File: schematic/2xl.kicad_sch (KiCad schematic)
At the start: 79 parts, among them J1 eye, J10 head+, J3 B-, J4 M-, J5 M+, J6 B+, J7 W, J9 head-, Q1 9014C, Q10 9014C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

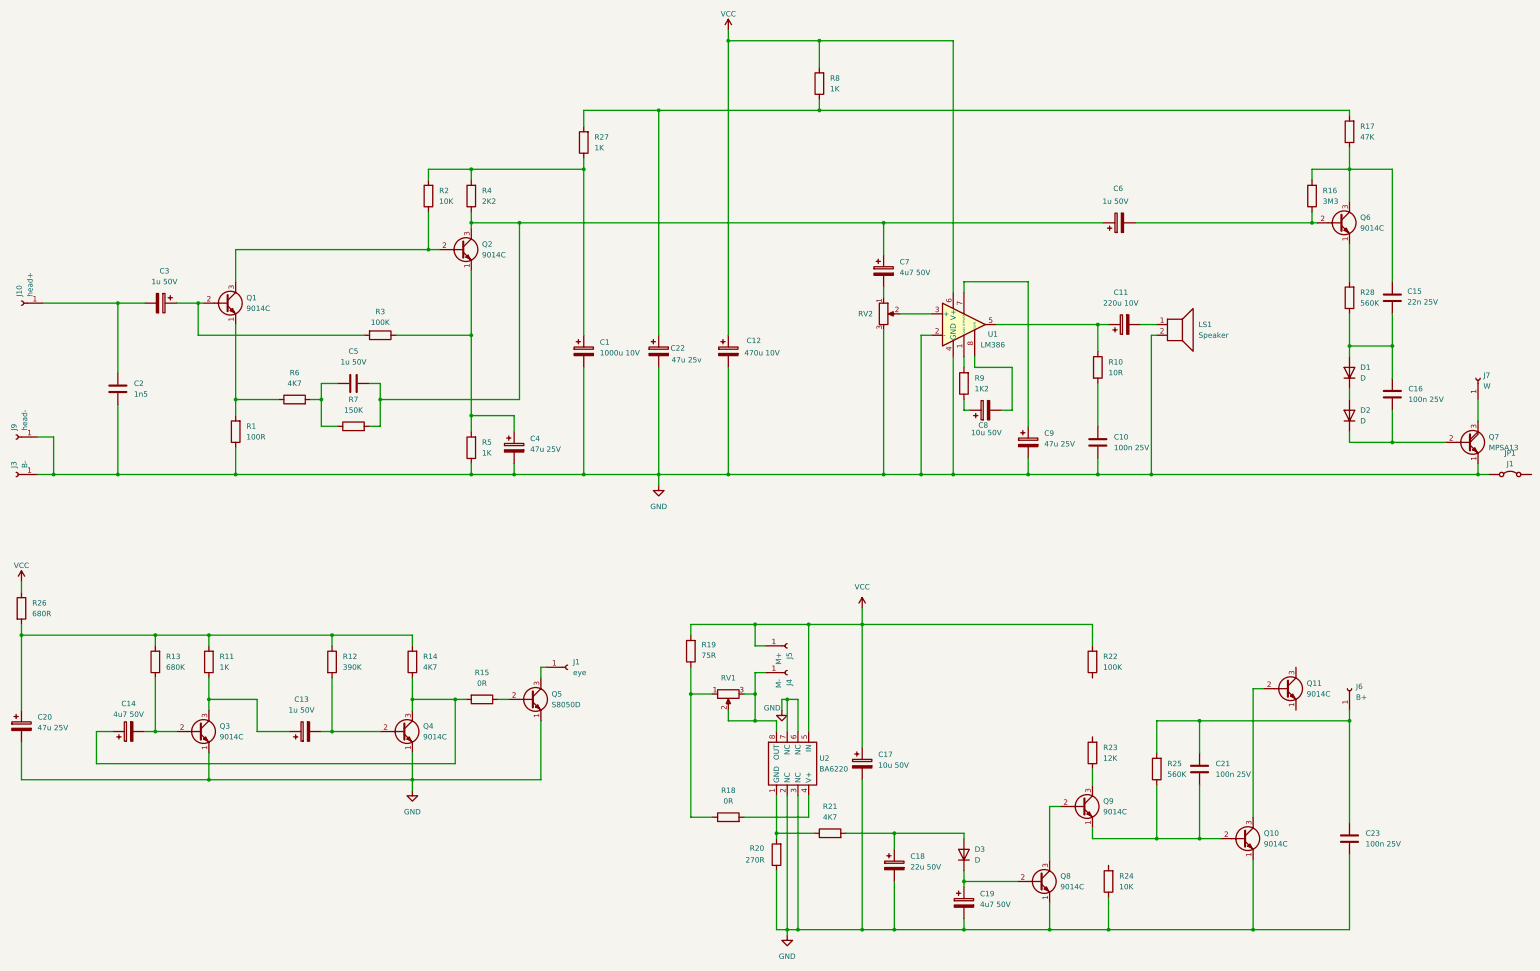
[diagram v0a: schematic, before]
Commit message: rearranged oscillator
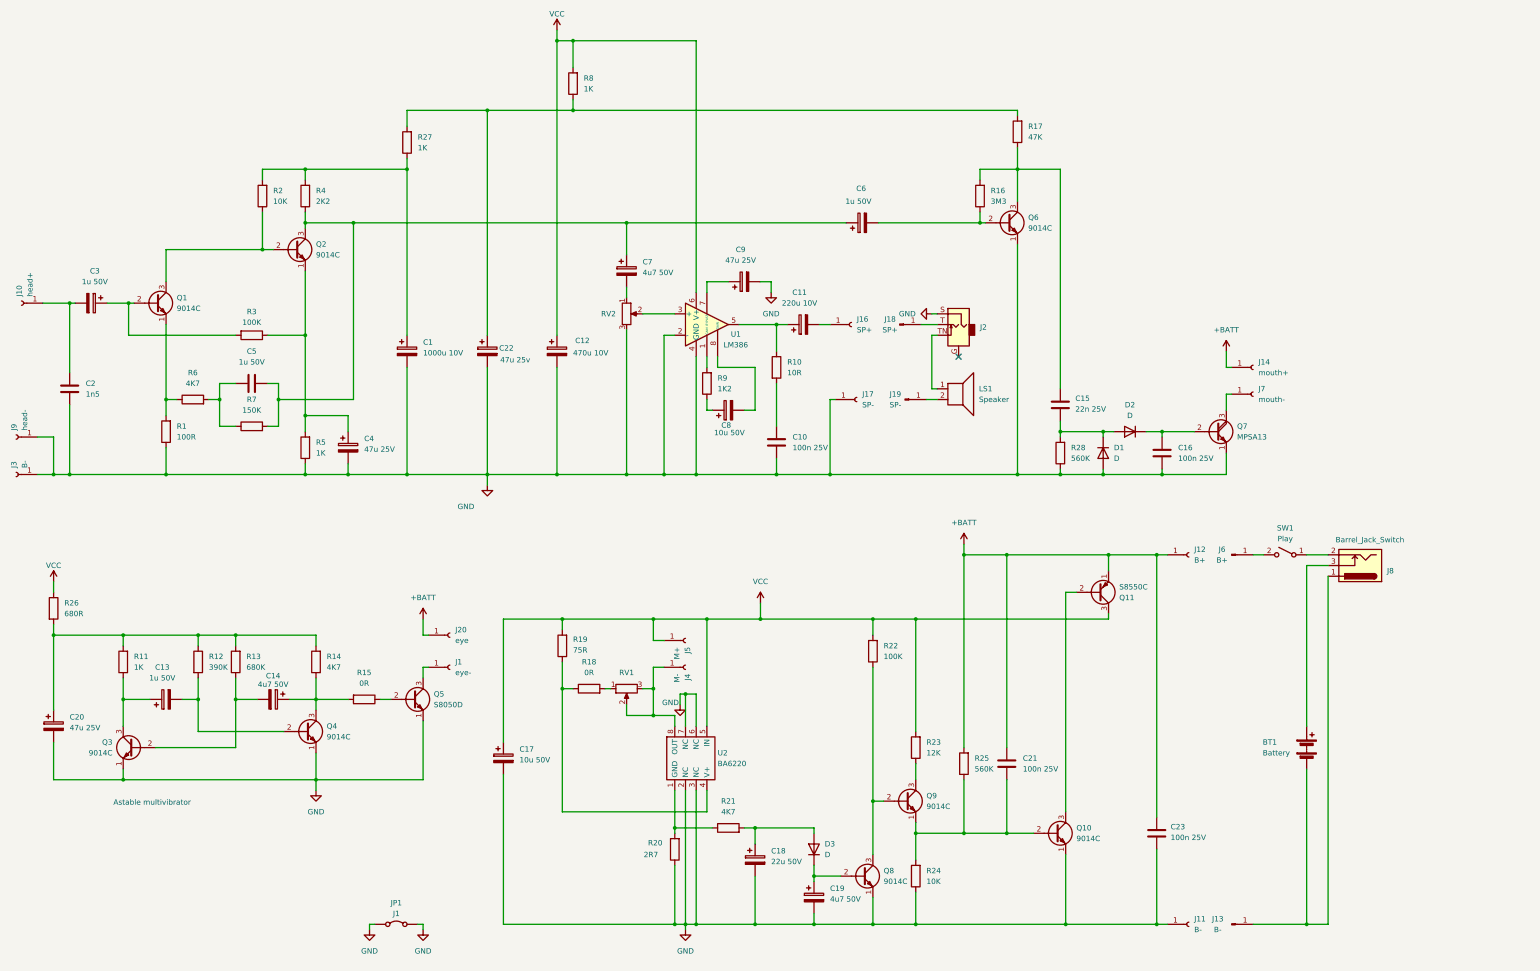
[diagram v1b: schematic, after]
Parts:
- removed J6: B+, symbol Connector:Conn_01x01_Socket
- removed Q11: 9014C, symbol Transistor_BJT:Q_NPN_EBC
- added BT1: Battery, symbol Device:Battery
- added J11: B-, symbol Connector:Conn_01x01_Socket
- added J12: B+, symbol Connector:Conn_01x01_Socket
- added J13: B-, symbol Connector:Conn_01x01_Pin
- added J14: mouth+, symbol Connector:Conn_01x01_Socket
- added J16: SP+, symbol Connector:Conn_01x01_Socket
- added J17: SP-, symbol Connector:Conn_01x01_Socket
- added J18: SP+, symbol Connector:Conn_01x01_Pin
- added J19: SP-, symbol Connector:Conn_01x01_Pin
- added J2: ~, symbol Connector_Audio:AudioJack2_Ground_SwitchT
- added J20: eye, symbol Connector:Conn_01x01_Socket
- added J6: B+, symbol Connector:Conn_01x01_Pin
- added J8: Barrel_Jack_Switch, symbol Connector:Barrel_Jack_Switch
- added Q11: S8550C, symbol Transistor_BJT:Q_PNP_EBC
- added SW1: Play, symbol Switch:SW_SPST
- J1: value eye -> eye-
- J7: value W -> mouth-
- R20: value 270R -> 2R7
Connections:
- net GND: now also C16.2, D1.2 (A), JP1.2 (B), Q6.1 (E), R28.1, J11.1 (Pin_1), J17.1 (Pin_1), J2.S; no longer LS1.2
- net VCC: now also R23.2, Q11.3 (C)
- net at R18.1, R19.1: now also U2.4 (V+); no longer RV1.1
- net at Q8.3 (C), Q9.2 (B): now also R22.1
- net at LS1.1: now also J2.TN; no longer C11.2
- net at D2.1 (K), Q7.2 (B): now also C16.1; no longer C16.2
- net +BATT: now reaches C21.1, C23.1, R25.2
- net +BATT: now also J12.1 (Pin_1), J14.1 (Pin_1), J20.1 (Pin_1), Q11.1 (E)
- net at R18.2: now also RV1.1; no longer U2.4 (V+)
- net at Q10.3 (C): now also Q11.2 (B)
- net at C21.2, Q10.2 (B), Q9.1 (E)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: now also R24.2
- net at R28.2: now also C15.2, D1.1 (K), D2.2 (A); no longer Q6.1 (E)
- new net: J8.2, SW1.1 (A)
- new net: J6.1 (Pin_1), SW1.2 (B)
- new net: J19.1 (Pin_1), LS1.2
- new net: C11.2, J16.1 (Pin_1)
- new net: BT1.2 (-), J13.1 (Pin_1), J8.1
- new net: BT1.1 (+), J8.3
- new net: J18.1 (Pin_1), J2.T
- no-connect marks 0 -> 1
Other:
- note added: "Astable multivibrator"
- moved on the sheet: C1, C10, C11, C12, C13, C14, C15, C16, C17, C18, C19, C2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
